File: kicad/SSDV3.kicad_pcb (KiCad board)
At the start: 4 copper layers, 58.4 x 28.8 mm, 71 parts, among them J1 SolderPad, J2 SolderPad, J3 SolderPad, J4 SolderPad, J5 SolderPad, J6 SolderPad, J7 SolderPad_01x02, J8 SolderPad_1x03, Q1 CSD19537Q3, Q2 CSD19537Q3, Q3 BSZ096N10LS5, U1 LM5050-1, U2 LM5146

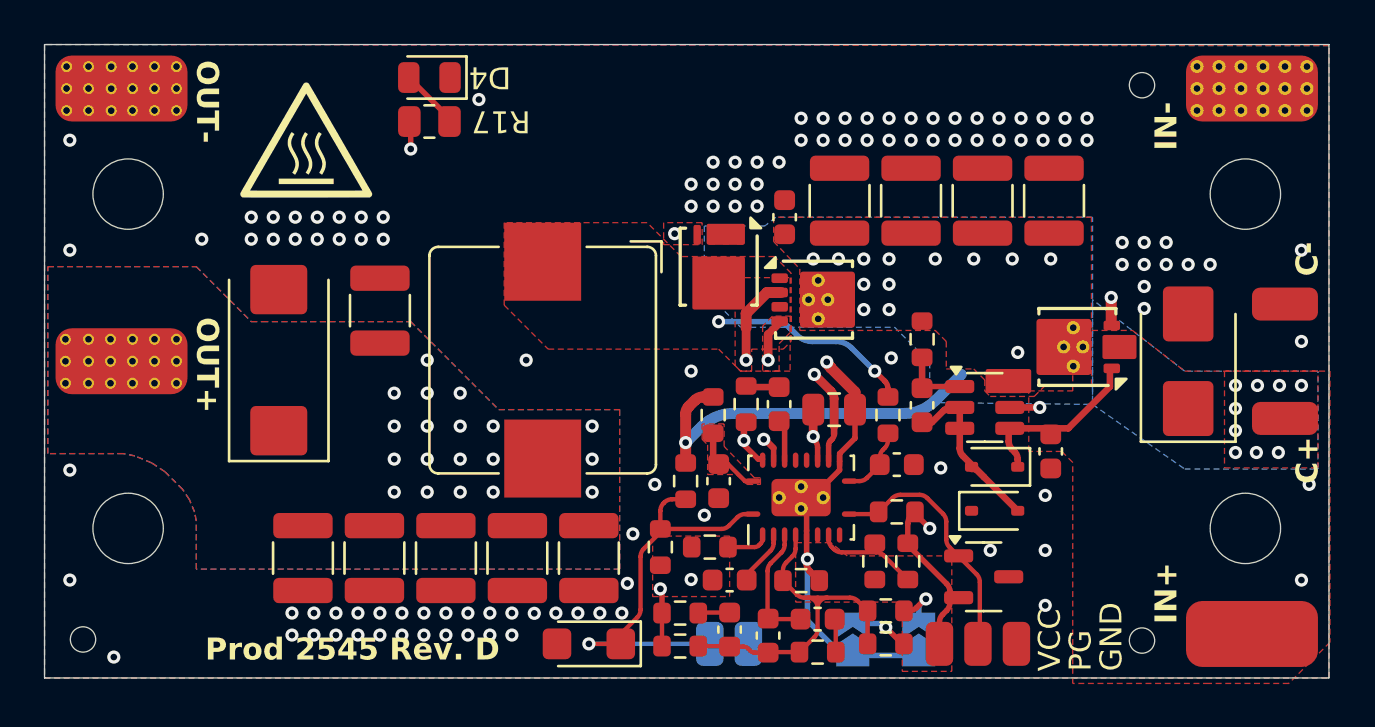
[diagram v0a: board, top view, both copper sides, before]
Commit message: Addressed HS FET failure mode from revC
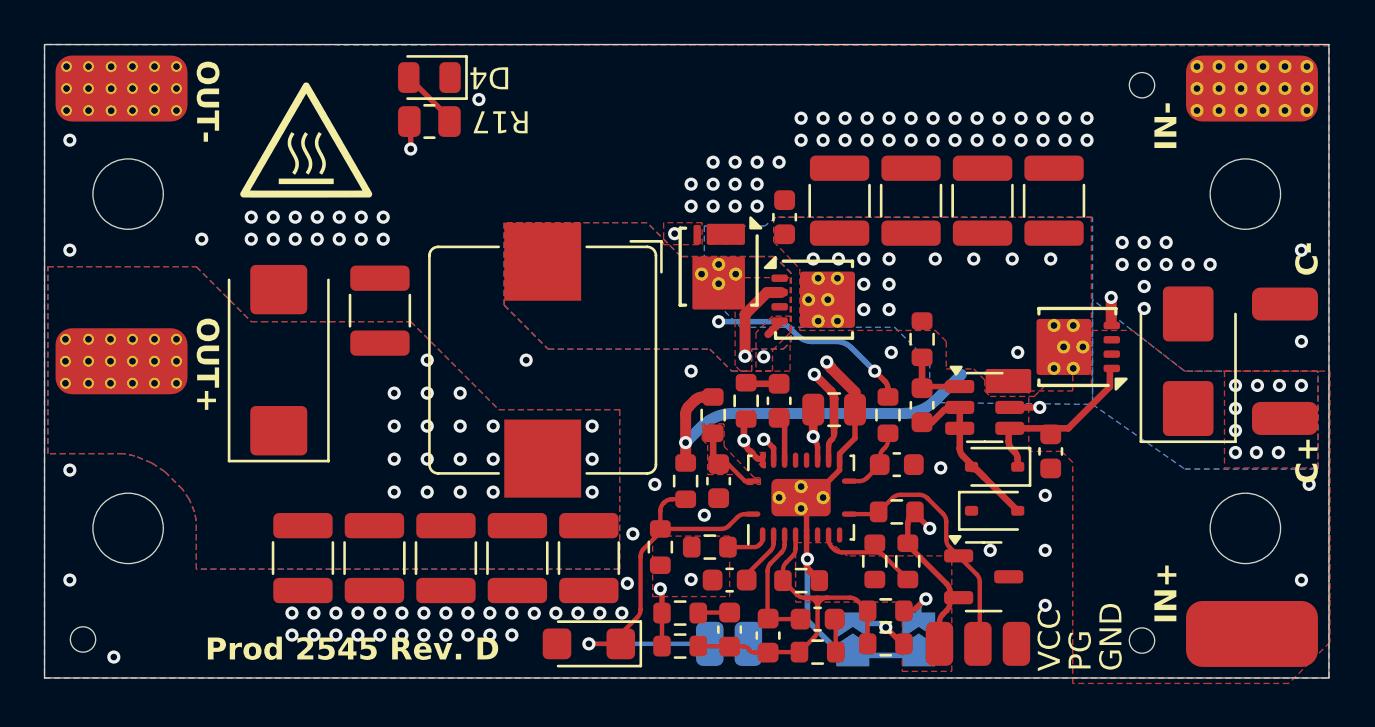
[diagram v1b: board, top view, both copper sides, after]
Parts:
- removed the H1 at (174.6, 122.0)
- removed the H2 at (174.6, 106.8)
- removed the H3 at (123.8, 122.0)
- removed H4: MountingHole, MountingHole:MountingHole_3.2mm_M3_ISO7380
- added HS1: 241802B92200G, Heatsink_JJ:24180xB9x200G, B.Cu at (149.2, 114.4)
- J7: value SolderPad_01x02 -> SolderPad_1x02
- Q3: footprint Package_SON_JJ:Infineon_PG-TSDSON-8-26_3.3x3.3mm_P0.65mm -> Package_SON_JJ:Infineon_PG-TSDSON-8-26_3.3x3.3mm_P0.65mm_ThermalVias-D0.3mm
- moved C15 0.15 mm to (153.4, 116.2)
- moved R15 0.15 mm to (151.9, 116.2)
- renumbered H5 to H1, H6 to H2, H7 to H3
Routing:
- net /buck_converter/LO: track 13.4 -> 15.0 mm
- net /buck_converter/HO: track 6.65 -> 5.50 mm
- net PGND: track 17.2 -> 18.2 mm
- added copper zone on B.Cu, net /buck_converter/SW
- added copper zone on In2.Cu, net /buck_converter/SW
